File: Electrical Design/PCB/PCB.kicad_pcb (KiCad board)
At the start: 2 copper layers, 50 x 150 mm, 60 parts, among them J1 Conn_02x03_Odd_Even, J2 10118193-0001LF, M1 Camera_Servo, M2 Release_Servo, Q1 LED_MOS, Q2 CAMERA_MOS, Q3 RELEASE_MOS, Q4 BUZZER_MOS, U1 ADP3338AKCZ-5-R7, U10 Adafruit_Cam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

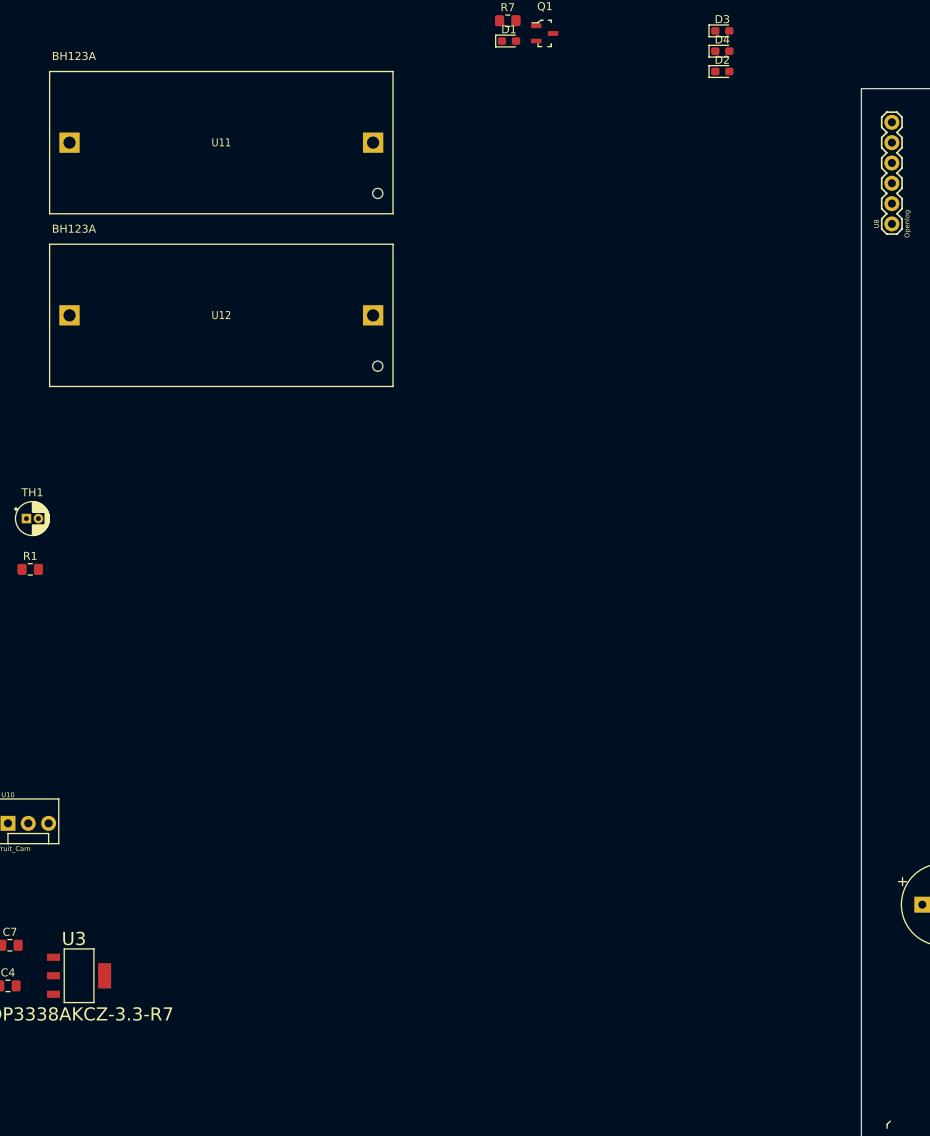
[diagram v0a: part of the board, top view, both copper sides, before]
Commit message: Fix Batteries
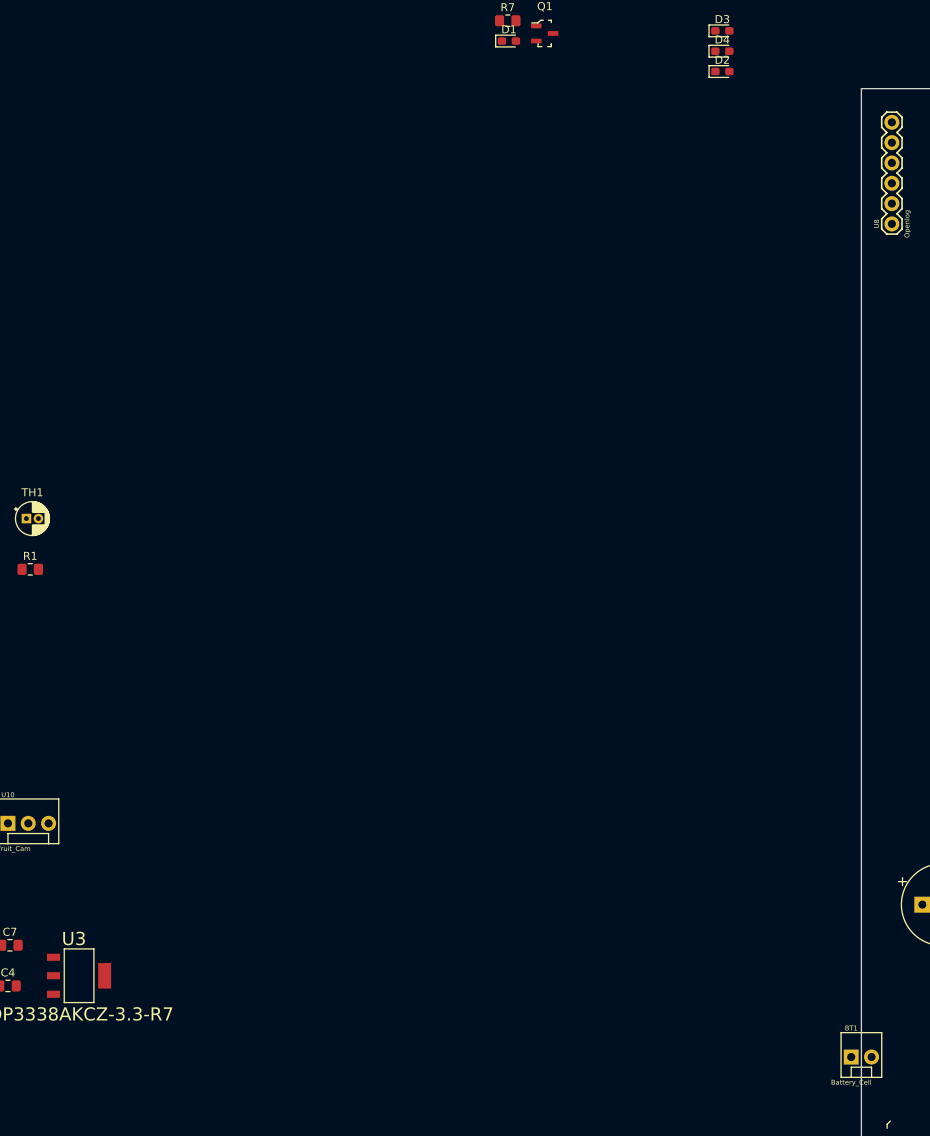
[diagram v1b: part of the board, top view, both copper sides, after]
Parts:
- removed U11, U12: BH123A, BH123A:BH123A
- added BT1: Battery_Cell, Connectors:MOLEX-1X2, F.Cu at (125.7, 146.1)
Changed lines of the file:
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@@
-(kicad_pcb (version 20171130) (host pcbnew 5.0.2-bee76a0~70~ubuntu18.04.1)
+(kicad_pcb (version 20171130) (host pcbnew "(5.0.1-3-g963ef8bb5)")
   (general
     (thickness 1.6)
@@
     (tracks 0)
     (zones 0)
-    (modules 60)
-    (nets 97)
+    (modules 59)
+    (nets 96)
   )
   (page A4)
@@
   (net 94 "Net-(U9-Pad44)")
   (net 95 /CAMERA_DATA)
-  (net 96 "Net-(U11-Pad-)")
   (net_class Default "This is the default net class."
     (clearance 0.1524)
@@
     (add_net "Net-(Q4-Pad1)")
     (add_net "Net-(R6-Pad2)")
-    (add_net "Net-(U11-Pad-)")
     (add_net "Net-(U2-Pad15)")
     (add_net "Net-(U2-Pad16)")
@@
     (add_net "Net-(U9-Pad7)")
   )
-  (module BH123A:BH123A (layer F.Cu)
-    (at 46.99 53.34)
-    (fp_text reference U12 (at 0 0) (layer F.SilkS)
-      (effects (font (size 1 0.9) (thickness 0.05)))
+  (module Connectors:MOLEX-1X2 (layer F.Cu)
+    (at 125.73 146.05)
+    (descr "MOLEX 2-PIN PLATED THROUGH-HOLE")
+    (tags "MOLEX 2-PIN PLATED THROUGH-HOLE")
+    (attr virtual)
+    (fp_text reference BT1 (at 0 -3.60426) (layer F.SilkS)
+      (effects (font (size 0.6096 0.6096) (thickness 0.127)))
     )
-    (fp_text value BH123A (at -18.415 -10.795) (layer F.SilkS)
-      (effects (font (size 1 1) (thickness 0.05)))
+    (fp_text value Battery_Cell (at 0 3.175) (layer F.SilkS)
+      (effects (font (size 0.6096 0.6096) (thickness 0.127)))
     )
-    (fp_text user BH123A (at -3.81 -1.27) (layer Cmts.User)
-      (effects (font (size 1 1) (thickness 0.05)))
-    )
-    (fp_line (start 21.463 8.89) (end 21.463 -8.89) (layer F.SilkS) (width 0.127))
-    (fp_line (start -21.463 8.89) (end 21.463 8.89) (layer F.SilkS) (width 0.127))
-    (fp_line (start -21.463 -8.89) (end -21.463 8.89) (layer F.SilkS) (width 0.127))
-    (fp_line (start 21.463 -8.89) (end -21.463 -8.89) (layer F.SilkS) (width 0.127))
-    (pad Hole np_thru_hole circle (at 19.558 6.35) (size 1.27 1.27) (drill 1.27) (layers *.Cu *.Mask F.SilkS))
-    (pad + thru_hole rect (at 18.9738 0) (size 2.54 2.54) (drill 1.524) (layers *.Cu *.Mask)
-      (net 96 "Net-(U11-Pad-)"))
-    (pad - thru_hole rect (at -18.9738 0) (size 2.54 2.54) (drill 1.524) (layers *.Cu *.Mask)
-      (net 1 GND))
-  )
-  (module BH123A:BH123A (layer F.Cu)
-    (at 46.99 31.75)
-    (fp_text reference U11 (at 0 0) (layer F.SilkS)
-      (effects (font (size 1 0.9) (thickness 0.05)))
-    )
-    (fp_text value BH123A (at -18.415 -10.795) (layer F.SilkS)
-      (effects (font (size 1 1) (thickness 0.05)))
-    )
-    (fp_line (start 21.463 -8.89) (end -21.463 -8.89) (layer F.SilkS) (width 0.127))
-    (fp_line (start -21.463 -8.89) (end -21.463 8.89) (layer F.SilkS) (width 0.127))
-    (fp_line (start -21.463 8.89) (end 21.463 8.89) (layer F.SilkS) (width 0.127))
-    (fp_line (start 21.463 8.89) (end 21.463 -8.89) (layer F.SilkS) (width 0.127))
-    (fp_text user BH123A (at -3.81 -1.27) (layer Cmts.User)
-      (effects (font (size 1 1) (thickness 0.05)))
-    )
-    (pad - thru_hole rect (at -18.9738 0) (size 2.54 2.54) (drill 1.524) (layers *.Cu *.Mask)
-      (net 96 "Net-(U11-Pad-)"))
-    (pad + thru_hole rect (at 18.9738 0) (size 2.54 2.54) (drill 1.524) (layers *.Cu *.Mask)
-      (net 2 +6V))
-    (pad Hole np_thru_hole circle (at 19.558 6.35) (size 1.27 1.27) (drill 1.27) (layers *.Cu *.Mask F.SilkS))
+    (fp_line (start -1.27 -3.048) (end -1.27 2.54) (layer F.SilkS) (width 0.127))
+    (fp_line (start 3.81 -3.048) (end 3.81 2.54) (layer F.SilkS) (width 0.127))
+    (fp_line (start 3.81 -3.048) (end -1.27 -3.048) (layer F.SilkS) (width 0.127))
+    (fp_line (start 3.81 2.54) (end 2.54 2.54) (layer F.SilkS) (width 0.127))
+    (fp_line (start 2.54 2.54) (end 0 2.54) (layer F.SilkS) (width 0.127))
+    (fp_line (start 0 2.54) (end -1.27 2.54) (layer F.SilkS) (width 0.127))
+    (fp_line (start 0 2.54) (end 0 1.27) (layer F.SilkS) (width 0.127))
+    (fp_line (start 0 1.27) (end 2.54 1.27) (layer F.SilkS) (width 0.127))
+    (fp_line (start 2.54 1.27) (end 2.54 2.54) (layer F.SilkS) (width 0.127))
+    (pad 1 thru_hole rect (at 0 0) (size 1.8796 1.8796) (drill 1.016) (layers *.Cu *.Mask)
+      (net 2 +6V) (solder_mask_margin 0.1016))
+    (pad 2 thru_hole circle (at 2.54 0) (size 1.8796 1.8796) (drill 1.016) (layers *.Cu *.Mask)
+      (net 1 GND) (solder_mask_margin 0.1016))
   )
   (module Connectors:MOLEX-1X3 (layer F.Cu)

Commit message: Start routing
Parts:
- U1: value ADP3338AKCZ-5-R7 -> 6V-->5V
- U3: value ADP3338AKCZ-3.3-R7 -> 6V-->3.3V
- moved Q1 161.2 mm to (137.2, 171.4), turned to 270 degrees
- moved D1 161.0 mm to (132.5, 172.2)
- moved R7 160.7 mm to (138.2, 167.4), turned to 270 degrees
- moved C4 152.5 mm to (169.4, 169.4), turned to 90 degrees
- moved D3 150.1 mm to (132.4, 166.1)
- moved C1 149.5 mm to (150.1, 169.4), turned to 90 degrees
- moved C7 148.7 mm to (167.1, 157.5)
- moved D2 148.1 mm to (132.5, 169.2)
- moved D4 144.6 mm to (132.4, 163.1)
- moved U1 141.3 mm to (147.8, 162.8), turned to 90 degrees
- moved U3 140.5 mm to (167.1, 162.8), turned to 90 degrees
- moved C6 137.2 mm to (147.8, 157.5)
- moved C10 111.4 mm to (26.9, 182.6)
- moved C9 111.4 mm to (26.9, 180.3)
- moved C2 111.4 mm to (59.9, 178.6)
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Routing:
- net +6V: track 0.00 -> 73.7 mm
- net +3V3: track 0.00 -> 53.3 mm, vias 0 -> 4
- net +5V: track 0.00 -> 20.1 mm
- net Net-(D1-Pad1): track 0.00 -> 7.05 mm
- net Net-(Q1-Pad1): track 0.00 -> 1.99 mm

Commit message: Fix Connector
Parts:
- J1: footprint Connector:Tag-Connect_TC2030-IDC-FP_2x03_P1.27mm_Vertical -> Connectors:2X3
- U1: value 6V-->5V -> ADP3338AKCZ-5-R7
- U3: value 6V-->3.3V -> ADP3338AKCZ-3.3-R7
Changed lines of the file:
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@@
-(kicad_pcb (version 20171130) (host pcbnew 5.0.2-bee76a0~70~ubuntu18.04.1)
+(kicad_pcb (version 20171130) (host pcbnew "(5.0.1-3-g963ef8bb5)")
   (general
     (thickness 1.6)
@@
     (add_net "Net-(U9-Pad7)")
   )
+  (module Connectors:2X3 (layer F.Cu)
+    (at 187.325 119.38)
+    (descr "PLATED THROUGH HOLE - 2X3")
+    (tags "PLATED THROUGH HOLE - 2X3")
+    (attr virtual)
+    (fp_text reference J1 (at 0 -4.445) (layer F.SilkS)
+      (effects (font (size 0.6096 0.6096) (thickness 0.127)))
+    )
+    (fp_text value Conn_02x03_Odd_Even (at 0 2.286) (layer F.SilkS)
+      (effects (font (size 0.6096 0.6096) (thickness 0.127)))
+    )
+    (fp_line (start -1.27 0.635) (end -0.635 1.27) (layer F.SilkS) (width 0.2032))
+    (fp_line (start 0.635 1.27) (end 1.27 0.635) (layer F.SilkS) (width 0.2032))
+    (fp_line (start 1.27 0.635) (end 1.905 1.27) (layer F.SilkS) (width 0.2032))
+    (fp_line (start 3.175 1.27) (end 3.81 0.635) (layer F.SilkS) (width 0.2032))
+    (fp_line (start 3.81 0.635) (end 4.445 1.27) (layer F.SilkS) (width 0.2032))
+    (fp_line (start 5.715 1.27) (end 6.35 0.635) (layer F.SilkS) (width 0.2032))
+    (fp_line (start -1.27 0.635) (end -1.27 -3.175) (layer F.SilkS) (width 0.2032))
+    (fp_line (start -1.27 -3.175) (end -0.635 -3.81) (layer F.SilkS) (width 0.2032))
+    (fp_line (start -0.635 -3.81) (end 0.635 -3.81) (layer F.SilkS) (width 0.2032))
+    (fp_line (start 0.635 -3.81) (end 1.27 -3.175) (layer F.SilkS) (width 0.2032))
+    (fp_line (start 1.27 -3.175) (end 1.905 -3.81) (layer F.SilkS) (width 0.2032))
+    (fp_line (start 1.905 -3.81) (end 3.175 -3.81) (layer F.SilkS) (width 0.2032))
+    (fp_line (start 3.175 -3.81) (end 3.81 -3.175) (layer F.SilkS) (width 0.2032))
+    (fp_line (start 3.81 -3.175) (end 4.445 -3.81) (layer F.SilkS) (width 0.2032))
+    (fp_line (start 4.445 -3.81) (end 5.715 -3.81) (layer F.SilkS) (width 0.2032))
+    (fp_line (start 5.715 -3.81) (end 6.35 -3.175) (layer F.SilkS) (width 0.2032))
+    (fp_line (start 1.27 -3.175) (end 1.27 0.635) (layer F.SilkS) (width 0.2032))
+    (fp_line (start 3.81 -3.175) (end 3.81 0.635) (layer F.SilkS) (width 0.2032))
+    (fp_line (start 6.35 -3.175) (end 6.35 0.635) (layer F.SilkS) (width 0.2032))
+    (fp_line (start 4.445 1.27) (end 5.715 1.27) (layer F.SilkS) (width 0.2032))
+    (fp_line (start 1.905 1.27) (end 3.175 1.27) (layer F.SilkS) (width 0.2032))
+    (fp_line (start -0.635 1.27) (end 0.635 1.27) (layer F.SilkS) (width 0.2032))
+    (fp_line (start 0.635 1.60274) (end -0.635 1.60274) (layer F.SilkS) (width 0.2032))
+    (fp_line (start -0.635 1.60274) (end 0.635 1.60274) (layer F.SilkS) (width 0.2032))
+    (pad 1 thru_hole circle (at 0 0) (size 1.8796 1.8796) (drill 1.016) (layers *.Cu *.Mask)
+      (net 11 /PDI_DATA) (solder_mask_margin 0.1016))
+    (pad 2 thru_hole circle (at 0 -2.54) (size 1.8796 1.8796) (drill 1.016) (layers *.Cu *.Mask)
+      (net 3 +3V3) (solder_mask_margin 0.1016))
+    (pad 3 thru_hole circle (at 2.54 0) (size 1.8796 1.8796) (drill 1.016) (layers *.Cu *.Mask)
+      (net 12 "Net-(J1-Pad3)") (solder_mask_margin 0.1016))
+    (pad 4 thru_hole circle (at 2.54 -2.54) (size 1.8796 1.8796) (drill 1.016) (layers *.Cu *.Mask)
+      (net 13 "Net-(J1-Pad4)") (solder_mask_margin 0.1016))
+    (pad 5 thru_hole circle (at 5.08 0) (size 1.8796 1.8796) (drill 1.016) (layers *.Cu *.Mask)
+      (net 14 /PDI_CLK) (solder_mask_margin 0.1016))
+    (pad 6 thru_hole circle (at 5.08 -2.54) (size 1.8796 1.8796) (drill 1.016) (layers *.Cu *.Mask)
+      (net 1 GND) (solder_mask_margin 0.1016))
+  )
   (module Connectors:MOLEX-1X2 (layer F.Cu)
     (at 156.718 168.148)
@@
     )
   )
-  (module Connector:Tag-Connect_TC2030-IDC-FP_2x03_P1.27mm_Vertical (layer F.Cu)
-    (at 187.325 119.38)
-    (descr "Tag-Connect programming header; http://www.tag-connect.com/Materials/TC2030-IDC.pdf")
-    (tags "tag connect programming header pogo pins")
-    (attr virtual)
-    (fp_text reference J1 (at 0 5) (layer F.SilkS)
-      (effects (font (size 1 1) (thickness 0.15)))
-    )
-    (fp_text value Conn_02x03_Odd_Even (at 0 -4.7) (layer F.Fab)
-      (effects (font (size 1 1) (thickness 0.15)))
-    )
-    (fp_text user KEEPOUT (at 0 0) (layer Cmts.User)
-      (effects (font (size 0.4 0.4) (thickness 0.07)))
-    )
-    (fp_line (start -1.27 0.635) (end -1.27 -0.635) (layer Dwgs.User) (width 0.1))
-    (fp_line (start 1.27 0.635) (end -1.27 0.635) (layer Dwgs.User) (width 0.1))
-    (fp_line (start 1.27 -0.635) (end 1.27 0.635) (layer Dwgs.User) (width 0.1))
-    (fp_line (start -1.27 -0.635) (end 1.27 -0.635) (layer Dwgs.User) (width 0.1))
-    (fp_line (start -1.905 1.27) (end -1.905 0.635) (layer F.SilkS) (width 0.12))
-    (fp_line (start -1.27 1.27) (end -1.905 1.27) (layer F.SilkS) (width 0.12))
-    (fp_line (start -4.25 4.25) (end -4.25 -4.25) (layer F.CrtYd) (width 0.05))
-    (fp_line (start 3.75 4.25) (end -4.25 4.25) (layer F.CrtYd) (width 0.05))
-    (fp_line (start 3.75 -4.25) (end 3.75 4.25) (layer F.CrtYd) (width 0.05))
-    (fp_line (start -4.25 -4.25) (end 3.75 -4.25) (layer F.CrtYd) (width 0.05))
-    (fp_text user %R (at 0 0) (layer F.Fab)
-      (effects (font (size 1 1) (thickness 0.15)))
-    )
-    (fp_line (start -1.27 0.635) (end 0 -0.635) (layer Dwgs.User) (width 0.1))
-    (fp_line (start -1.27 0) (end -0.635 -0.635) (layer Dwgs.User) (width 0.1))
-    (fp_line (start -0.635 0.635) (end 0.635 -0.635) (layer Dwgs.User) (width 0.1))
-    (fp_line (start 0 0.635) (end 1.27 -0.635) (layer Dwgs.User) (width 0.1))
-    (fp_line (start 0.635 0.635) (end 1.27 0) (layer Dwgs.User) (width 0.1))
-    (pad "" np_thru_hole circle (at -2.54 2.54) (size 2.3749 2.3749) (drill 2.3749) (layers *.Cu *.Mask))
-    (pad "" np_thru_hole circle (at -2.54 -2.54) (size 2.3749 2.3749) (drill 2.3749) (layers *.Cu *.Mask))
-    (pad "" np_thru_hole circle (at 0.635 -2.54) (size 2.3749 2.3749) (drill 2.3749) (layers *.Cu *.Mask))
-    (pad "" np_thru_hole circle (at 0.635 2.54) (size 2.3749 2.3749) (drill 2.3749) (layers *.Cu *.Mask))
-    (pad "" np_thru_hole circle (at 2.54 -1.016) (size 0.9906 0.9906) (drill 0.9906) (layers *.Cu *.Mask))
-    (pad "" np_thru_hole circle (at 2.54 1.016) (size 0.9906 0.9906) (drill 0.9906) (layers *.Cu *.Mask))
-    (pad "" np_thru_hole circle (at -2.54 0) (size 0.9906 0.9906) (drill 0.9906) (layers *.Cu *.Mask))
-    (pad 1 connect circle (at -1.27 0.635) (size 0.7874 0.7874) (layers F.Cu F.Mask)
-      (net 11 /PDI_DATA))
-    (pad 2 connect circle (at -1.27 -0.635) (size 0.7874 0.7874) (layers F.Cu F.Mask)
-      (net 3 +3V3))
-    (pad 3 connect circle (at 0 0.635) (size 0.7874 0.7874) (layers F.Cu F.Mask)
-      (net 12 "Net-(J1-Pad3)"))
-    (pad 4 connect circle (at 0 -0.635) (size 0.7874 0.7874) (layers F.Cu F.Mask)
-      (net 13 "Net-(J1-Pad4)"))
-    (pad 5 connect circle (at 1.27 0.635) (size 0.7874 0.7874) (layers F.Cu F.Mask)
-      (net 14 /PDI_CLK))
-    (pad 6 connect circle (at 1.27 -0.635) (size 0.7874 0.7874) (layers F.Cu F.Mask)
-      (net 1 GND))
-  )
   (module digikey-footprints:USB_Micro_B_Female_10118193-0001LF (layer F.Cu)
     (at 201.27 71.03)
@@
       (effects (font (size 1.64061 1.64061) (thickness 0.05)))
     )
-    (fp_text value 6V-->5V (at -0.5084 4.8298 90) (layer F.SilkS)
+    (fp_text value ADP3338AKCZ-5-R7 (at -0.5084 4.8298 90) (layer F.SilkS)
       (effects (font (size 1.64129 1.64129) (thickness 0.05)))
     )
@@
       (effects (font (size 1.64087 1.64087) (thickness 0.05)))
     )
-    (fp_text value 6V-->3.3V (at -0.508485 4.83074 90) (layer F.SilkS)
+    (fp_text value ADP3338AKCZ-3.3-R7 (at -0.508485 4.83074 90) (layer F.SilkS)
       (effects (font (size 1.64161 1.64161) (thickness 0.05)))
     )

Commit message: Were making progress
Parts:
- U1: value ADP3338AKCZ-5-R7 -> 6V-->5V
- U3: value ADP3338AKCZ-3.3-R7 -> 6V-->3.3V
- moved C11 153.6 mm to (140.5, 32.3), turned to 180 degrees
- moved U6 153.3 mm to (135.6, 32.3), turned to 180 degrees
- moved TH1 150.4 mm to (173.0, 82.3), turned to 270 degrees
- moved R1 145.1 mm to (168.1, 83.0), turned to 270 degrees
- moved C9 131.0 mm to (142.2, 118.1), turned to 270 degrees
- moved C10 129.3 mm to (138.9, 118.1), turned to 270 degrees
- moved C12 122.0 mm to (146.5, 126.0), turned to 180 degrees
- moved MOD1 118.8 mm to (146.1, 128.3), turned to 0 degrees
- moved U10 118.1 mm to (131.3, 157.2), turned to 90 degrees
- moved U5 114.8 mm to (145.5, 131.1), turned to 270 degrees
- moved U2 106.4 mm to (146.4, 137.9), turned to 0 degrees
- moved Q4 99.1 mm to (147.6, 88.2), turned to 270 degrees
- moved C2 97.5 mm to (152.4, 147.6), turned to 270 degrees
- moved LS1 97.2 mm to (150.6, 97.4)
- moved R14 93.1 mm to (147.6, 84.6)
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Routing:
- net +3V3: track 53.3 -> 219.3 mm, vias 4 -> 9
- net +6V: track 73.7 -> 161.9 mm, vias 0 -> 2
- net /MCU_VCC: track 0.00 -> 80.1 mm
- net /PA6-Therm: track 0.00 -> 35.7 mm
- net /MISO: track 0.00 -> 28.2 mm, vias 0 -> 3
- net /MCU_AVCC: track 0.00 -> 25.8 mm
- net /PA7-Voltage: track 0.00 -> 24.7 mm
- net /MOSI: track 0.00 -> 16.8 mm, vias 0 -> 1
- net Net-(C5-Pad1): track 0.00 -> 14.9 mm
- net Net-(LS1-PadN): track 0.00 -> 3.17 mm
- net Net-(Q4-Pad1): track 0.00 -> 2.54 mm
- net /~SS_5607: track 0.00 -> 2.40 mm
- net +5V: track 20.1 -> 17.8 mm

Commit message: Update
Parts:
- J1: value Conn_02x03_Odd_Even -> PDI Interface
- moved M2 125.4 mm to (138.8, 71.9), turned to 180 degrees
- moved M1 119.2 mm to (138.8, 60.2), turned to 180 degrees
- moved R11 114.6 mm to (143.0, 66.3), turned to 180 degrees
- moved R9 113.4 mm to (147.1, 71.6), turned to 180 degrees
- moved Q3 112.7 mm to (143.0, 70.7), turned to 180 degrees
- moved R8 110.7 mm to (142.8, 58.4), turned to 180 degrees
- moved R10 110.3 mm to (142.8, 56.4), turned to 180 degrees
- moved Q2 102.8 mm to (146.7, 57.4), turned to 180 degrees
- moved R2 63.8 mm to (131.1, 80.5)
- moved J1 61.6 mm to (132.8, 90.7), turned to 90 degrees
- moved R12 28.1 mm to (137.7, 109.2)
- moved R13 28.1 mm to (137.7, 106.7)
- moved C11 2.55 mm to (140.7, 34.8)
- moved U6 2.55 mm to (135.9, 34.8)
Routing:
- net +6V: track 161.9 -> 223.2 mm
- net +5V: track 17.8 -> 33.4 mm
